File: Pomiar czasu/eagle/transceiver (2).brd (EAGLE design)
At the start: 112.4 x 62.2 mm, 65 parts, among them IC1 MEGA8-AI, IC2 LF33, IC3 LF50, U1 RFM69HW

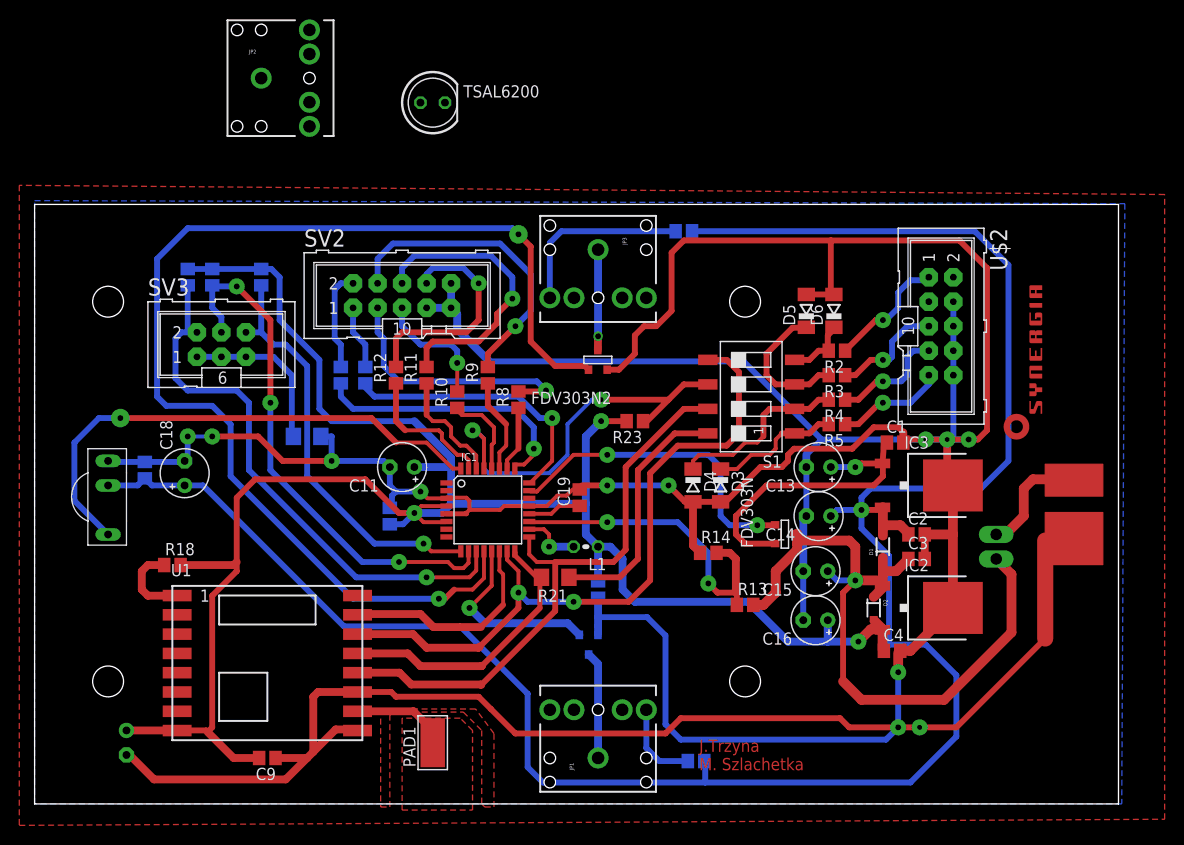
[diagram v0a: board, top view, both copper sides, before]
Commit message: RFM69:communication master->sensor works!
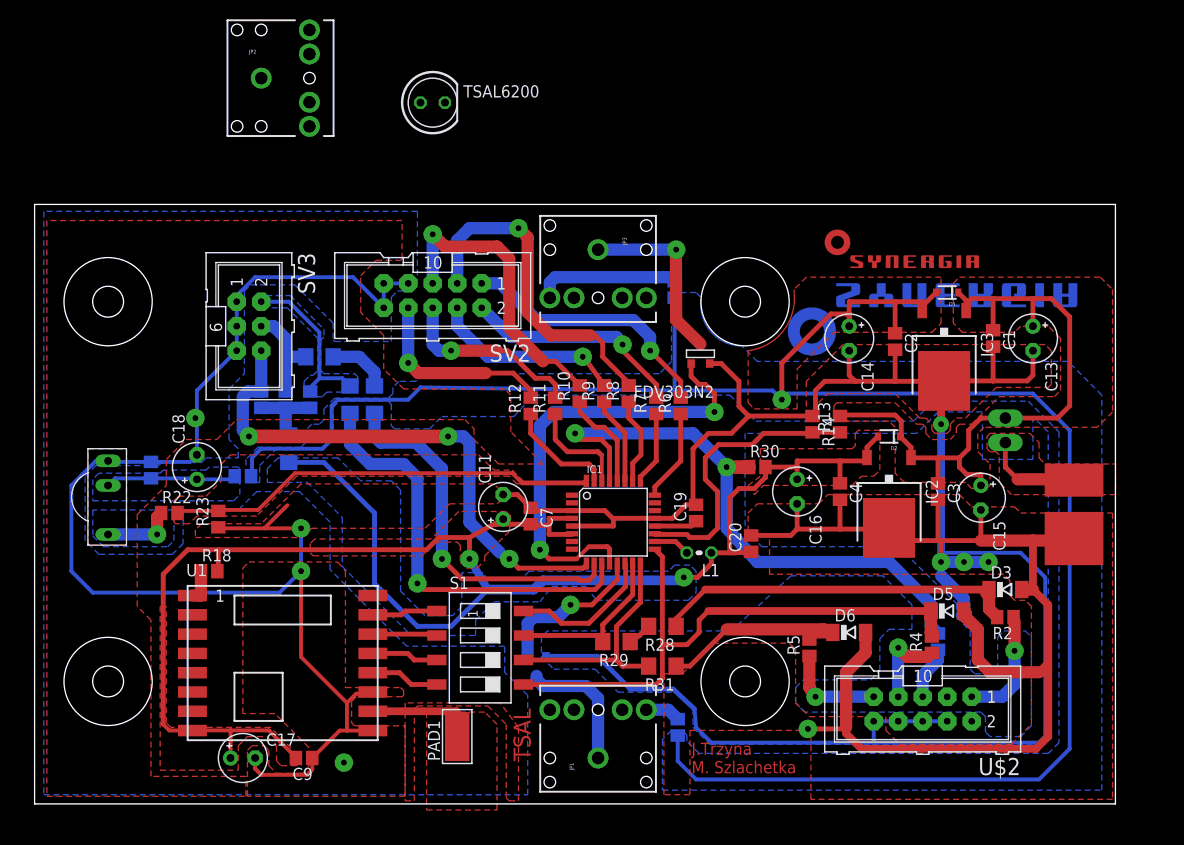
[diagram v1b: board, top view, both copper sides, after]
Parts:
- removed FDV303N: (no value), zetex:SOT-23
- added R22: 330k, resistor:R0805
- added R28, R29, R31, R32, R33, R35: 0R, rcl:R1206
- added R30: 10k, resistor:R0805
- added U$4: (no value), synergia_logo:SYNERGIA_30MM
- C1, C10, C19, C2, C20, C3, C4, C7, C9: value (none) -> 100n
- C11, C17: value (none) -> 22u
- C13, C14, C15, C16: value (none) -> 47u
- C18: value (none) -> 4,7u
- R2, R3, R4, R5: value (none) -> 330k
- R21: value 0R -> 220R; device rcl:R1206 -> resistor:R0805
- R23: value 1k -> 820k
- moved R23 44.4 mm to (19.1, 27.0), turned to 90 degrees
- moved U$2 39.7 mm to (92.1, 7.30), turned to 180 degrees
- moved S1 38.3 mm to (46.2, 13.7), turned to 270 degrees
- moved D5 34.4 mm to (94.6, 17.5), turned to 0 degrees
- moved R21 34.0 mm to (21.6, 31.4), flipped to the bottom
- moved D6 33.4 mm to (84.5, 15.2), turned to 0 degrees
- moved R6 32.9 mm to (67.0, 38.7), flipped to the top
- moved R7 32.9 mm to (64.5, 38.7), flipped to the top
- moved R2 32.7 mm to (100.6, 16.8)
- moved D3 31.4 mm to (100.6, 19.7), turned to 0 degrees
- moved R3 29.5 mm to (93.7, 14.3), flipped to the bottom, turned to 90 degrees
- moved D4 29.4 mm to (94.6, 17.5), flipped to the bottom, turned to 180 degrees
- moved U$3 28.7 mm to (81.9, 53.0), turned to 0 degrees
- moved R4 27.2 mm to (93.0, 14.0), turned to 90 degrees
- moved D1 27.2 mm to (94.6, 50.5), turned to 180 degrees
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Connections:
- removed net 5V_ENABLE: FDV303N.3, IC1.23
- removed net N$24: R21.1, S1.8
- new net N$25: C10.1, C18.+, R21.1, TSOP.V+
- new net N$33: R16.1, R33.2, SV3.4
- new net N$35: R33.1, R35.2
- new net N$36: S1.3, U1.13
- new net N$37: S1.2, U1.14
- new net N$38: S1.4, U1.12
- new net N$39: S1.1, U1.15
- net +3V3: now also R20.2, R30.2; no longer R15.2, R16.2, R17.2, R23.2
- net +5V: now also R21.2; no longer C10.2, C18.+, TSOP.V+
- net GND: now also C10.2, R23.1, SV3.1, SV3.3, SV3.5; no longer C10.1, R20.1
- net MISO: now also R31.2, S1.6; no longer R21.2, U1.13
- net MOSI: now also R29.2, S1.7; no longer S1.5, U1.14
- net N$1: now also R22.1, TSOP.OUT; no longer C1.1, C13.+, FDV303N.2, IC3.1
- net N$23: now also R15.2, R16.2, R17.2, R20.1; no longer R20.2, SV3.1, SV3.3, SV3.5
- net N$27: now also C1.1, C13.+, IC3.1; no longer FDV303N.1
- net N$29: now also R28.2, R29.1; no longer D6.C, R2.2, S1.4
- net N$30: now also D3.C, R2.2, R28.1; no longer D5.C, R3.2, S1.3
- net N$31: now also D6.C, R31.1, R5.2; no longer D4.C, R4.2, S1.2
- net N$32: now also R15.1, R32.2, SV3.2; no longer D3.C, R5.2, S1.1
- net RESET: now also D4.C, R3.2, R30.1; no longer R23.1, S1.6
- net SCK: now also D5.C, R4.2, S1.5; no longer S1.7, U1.12
- net SS: now also S1.8; no longer U1.15
- net SWITCH_DOWN: now also R32.1; no longer R15.1, SV3.2
- net SWITCH_OK: now also R35.1; no longer R16.1, SV3.4
- net TSOP_OUT: now also R22.2, R23.2; no longer TSOP.OUT
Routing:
- net LED_STRIPE: track 121.6 -> 47.7 mm
- net MOSI: track 72.4 -> 17.8 mm, vias 2 -> 0
- net 5V_ENABLE: track 33.0 -> 0.00 mm, vias 2 -> 0
- net N$1: track 33.5 -> 7.48 mm
- net N$24: track 26.0 -> 0.00 mm
- net GND: track 511.4 -> 486.3 mm, vias 12 -> 9
- net +3V3: track 209.1 -> 184.0 mm, vias 3 -> 2
- net N$30: track 14.7 -> 38.1 mm
- net LED2: track 28.3 -> 7.60 mm, vias 1 -> 0
- net N$9: track 6.66 -> 27.4 mm, vias 0 -> 1
- net RESET: track 41.9 -> 61.3 mm
- net LED1: track 28.9 -> 9.53 mm, vias 1 -> 0
- net N$13: track 12.9 -> 31.0 mm
- net SWITCH_OK: track 54.5 -> 38.2 mm, vias 3 -> 1
- net SWITCH_DOWN: track 58.6 -> 44.2 mm
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- added copper zone on layer 1, net +3V3
- added copper zone on layer 16, net +3V3
- added copper zone on layer 1, net +5V
- added copper zone on layer 16, net +5V
- added copper zone on layer 16, net N$1
- added copper zone on layer 1, net N$19
- added copper zone on layer 16, net N$25
- added copper zone on layer 1, net N$27
- added copper zone on layer 16, net N$32
- added copper zone on layer 1, net N$34
- added copper zone on layer 1, net TSOP_OUT
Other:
- board size 112.4 x 62.2 mm -> 112.1 x 62.2 mm
- board text added: "TSAL"

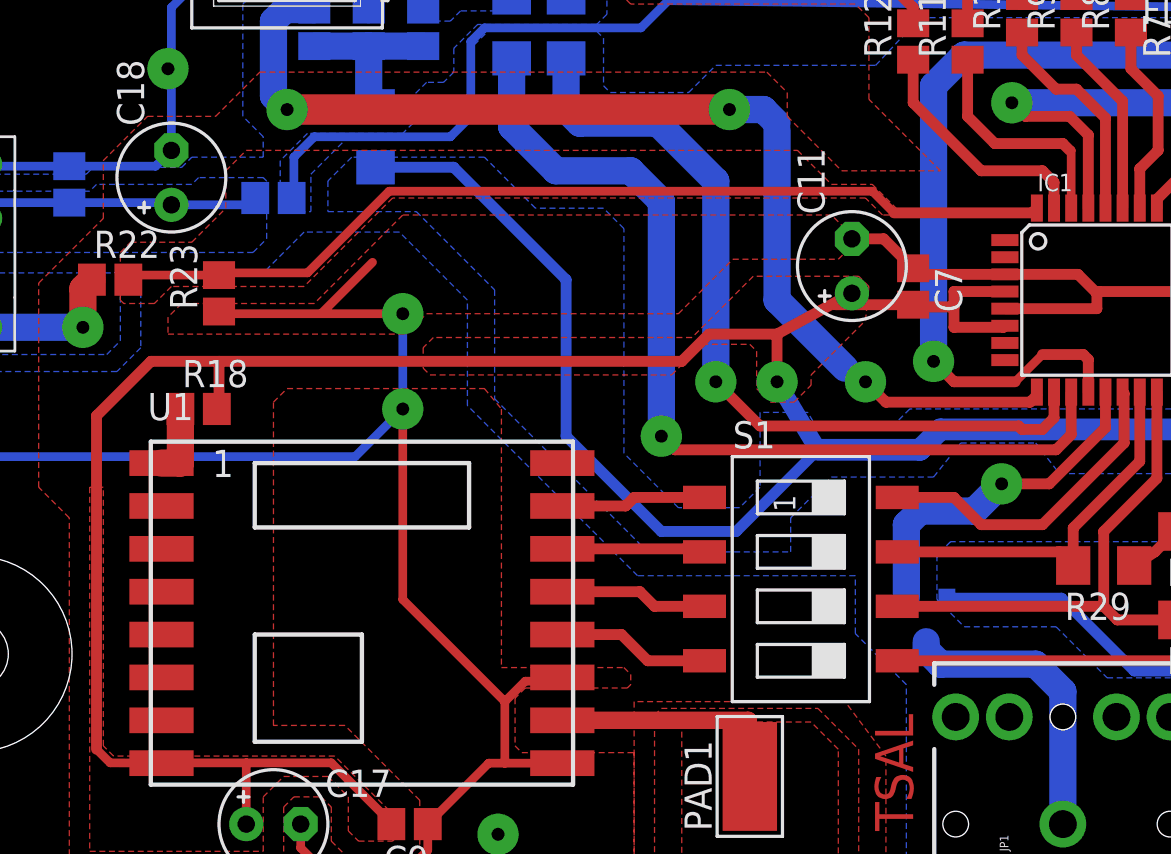
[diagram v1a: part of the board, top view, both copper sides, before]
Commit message: Channel: 442MHz(!!), ping with acknowledgement
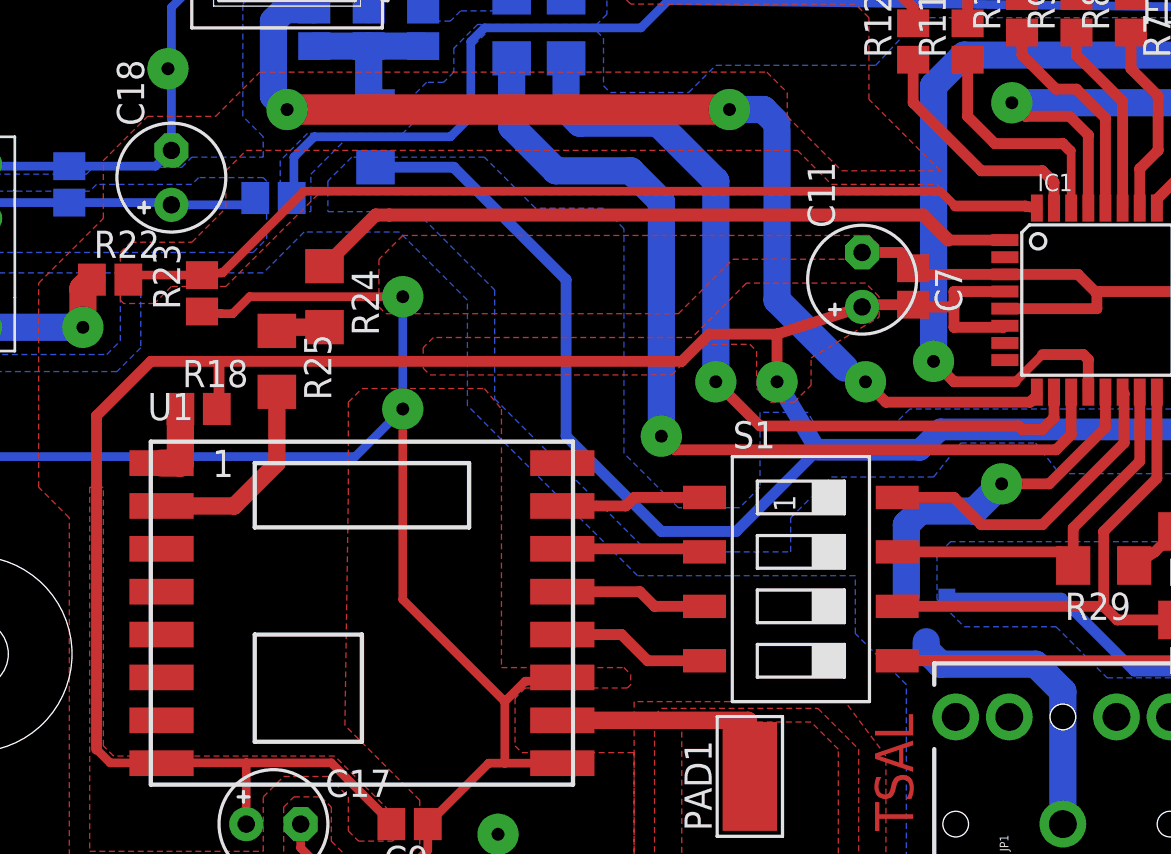
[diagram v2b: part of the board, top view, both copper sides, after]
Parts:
- added R24, R25: 0R, rcl:R1206
- moved C11 0.79 mm to (49.1, 27.6)
- moved R23 0.79 mm to (18.3, 27.0)
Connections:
- new net DIO0: IC1.1, R24.1
- new net N$24: R24.2, R25.1
- new net N$45: R25.2, U1.2
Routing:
- net DIO0: track 0.00 -> 33.4 mm
- net N$45: track 0.00 -> 9.54 mm
- net N$24: track 0.00 -> 2.29 mm
- net GND: track 486.3 -> 484.1 mm
- net +3V3: track 184.0 -> 182.1 mm

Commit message: final v1.0
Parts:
- removed R23: 820k, resistor:R0805
- added D7: (no value), diode:SOD80C
- R40: value 330k -> 220R
- moved R1 70.2 mm to (35.1, 68.1), turned to 0 degrees
- renumbered R22 to R40
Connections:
- net +5V: now also JP1.TIP; no longer R1.2
- net GND: now also D7.A; no longer R23.1
- net N$3: now also R1.2; no longer TSAL6200.A
- net N$8: now also TSAL6200.A; no longer JP1.TIP
- net TSOP_OUT: now also D7.C; no longer R23.2
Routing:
- net +5V: track 212.4 -> 216.9 mm
- net N$8: track 3.66 -> 0.00 mm
- net TSOP_OUT: track 44.4 -> 43.1 mm
- net GND: track 484.1 -> 483.5 mm
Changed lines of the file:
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@@
 <element name="TSOP" library="tsop" package="TSOP17XX" value="TSOP1736" x="7.62" y="29.21" rot="R270"/>
 <element name="TSAL6200" library="led" package="LED5MM" value="" x="41.275" y="70.1675"/>
-<element name="R1" library="resistor" package="R0805" value="36,5R" x="66.675" y="5.3975" rot="MR270"/>
+<element name="R1" library="resistor" package="R0805" value="36,5R" x="35.08375" y="68.10375" rot="MR0"/>
 <element name="U1" library="SparkFun-RF" package="RFM69W-XXXS2" value="RFM69HW" x="25.7175" y="12.065"/>
 <element name="U$2" library="con-harting-ml" package="ML10" value="" x="92.075" y="7.3025" rot="R180">
@@
 </element>
 <element name="R20" library="rcl" package="R1206" value="0R" x="26.3525" y="34.29" rot="MR270"/>
-<element name="R22" library="resistor" package="R0805" value="330k" x="13.97" y="27.6225"/>
+<element name="R40" library="resistor" package="R0805" value="220R" x="13.97" y="27.6225"/>
 <element name="R21" library="resistor" package="R0805" value="220R" x="21.59" y="31.4325" rot="MR180"/>
-<element name="R23" library="resistor" package="R0805" value="820k" x="18.25625" y="26.9875" rot="R90"/>
 <element name="R28" library="rcl" package="R1206" value="0R" x="65.0875" y="15.875" rot="R180"/>
 <element name="R31" library="rcl" package="R1206" value="0R" x="65.0875" y="11.7475" rot="R180"/>
@@
 <element name="R24" library="rcl" package="R1206" value="0R" x="23.97125" y="26.82875" rot="R270"/>
 <element name="R25" library="rcl" package="R1206" value="0R" x="21.74875" y="23.8125" rot="R270"/>
+<element name="D7" library="diode" package="SOD80C" value="" x="17.30375" y="25.55875"/>
 </elements>
 <signals>
 <signal name="+5V">
 <contactref element="R19" pad="2"/>
-<contactref element="R1" pad="2"/>
 <contactref element="C2" pad="1"/>
 <contactref element="C14" pad="+"/>
@@
 <wire x1="76.5175" y1="40.3225" x2="77.47" y2="39.37" width="0.4064" layer="16"/>
 <wire x1="66.3575" y1="49.95" x2="66.3575" y2="40.3225" width="0.4064" layer="16"/>
-<wire x1="66.675" y1="4.5475" x2="66.675" y2="1.905" width="0.4064" layer="16"/>
-<wire x1="66.675" y1="1.905" x2="68.58" y2="0" width="0.4064" layer="16"/>
+<wire x1="66.675" y1="1.905" x2="67.071875" y2="1.508125" width="0.4064" layer="16"/>
+<wire x1="67.071875" y1="1.508125" x2="68.58" y2="0" width="0.4064" layer="16"/>
 <wire x1="68.58" y1="0" x2="104.14" y2="0" width="0.4064" layer="16"/>
 <wire x1="104.14" y1="0" x2="107.315" y2="3.175" width="0.4064" layer="16"/>
@@
 </polygon>
 <polygon width="0.2032" layer="16">
-<vertex x="66.04" y="5.08"/>
-<vertex x="65.0875" y="4.1275"/>
-<vertex x="65.0875" y="-1.11125"/>
+<vertex x="62.5475" y="8.09625"/>
+<vertex x="62.5475" y="-0.9525"/>
 <vertex x="110.64875" y="-1.11125"/>
 <vertex x="110.64875" y="39.84625"/>
@@
 <vertex x="106.20375" y="3.81"/>
 <vertex x="105.0925" y="2.69875"/>
-<vertex x="68.8975" y="2.69875"/>
-<vertex x="67.6275" y="3.96875"/>
-<vertex x="67.6275" y="4.60375"/>
+<vertex x="69.5325" y="2.69875"/>
 <vertex x="67.15125" y="5.08"/>
-</polygon>
+<vertex x="67.15125" y="6.50875"/>
+<vertex x="65.56375" y="8.09625"/>
+</polygon>
+<contactref element="JP1" pad="TIP"/>
+<wire x1="63.42" y1="7.2225" x2="63.42" y2="5.16" width="1.016" layer="16"/>
+<wire x1="63.42" y1="5.16" x2="67.071875" y2="1.508125" width="1.016" layer="16"/>
 </signal>
 <signal name="+3V3">
@@
 <signal name="TSOP_OUT">
 <contactref element="IC1" pad="32"/>
-<contactref element="R22" pad="2"/>
-<contactref element="R23" pad="2"/>
+<contactref element="R40" pad="2"/>
 <wire x1="14.82" y1="27.6225" x2="15.035" y2="27.8375" width="0.4064" layer="1"/>
-<wire x1="15.035" y1="27.8375" x2="18.25625" y2="27.8375" width="0.4064" layer="1"/>
-<wire x1="18.25625" y1="27.8375" x2="19.1525" y2="27.94" width="0.4064" layer="1"/>
 <wire x1="19.1525" y1="27.94" x2="19.20875" y2="27.94" width="0.4064" layer="1"/>
 <wire x1="19.20875" y1="27.94" x2="23.01875" y2="31.75" width="0.4064" layer="1"/>
@@
 <wire x1="57.2075" y1="30.9626" x2="56.6674" y2="31.0575" width="0.508" layer="1"/>
 <wire x1="56.6674" y1="31.0575" x2="53.3975" y2="31.0575" width="0.508" layer="1"/>
+<contactref element="D7" pad="C"/>
+<wire x1="15.60375" y1="25.55875" x2="15.60375" y2="27.57625" width="0.4064" layer="1"/>
+<wire x1="15.60375" y1="27.57625" x2="15.5575" y2="27.6225" width="0.4064" layer="1"/>
+<wire x1="15.5575" y1="27.6225" x2="14.82" y2="27.6225" width="0.4064" layer="1"/>
 </signal>
 <signal name="MOSI">
@@
 </polygon>
 </signal>
-<signal name="N$8">
-<contactref element="R1" pad="1"/>
-<contactref element="JP1" pad="TIP"/>
-<wire x1="63.42" y1="7.2225" x2="65.7" y2="7.2225" width="1.27" layer="16"/>
-<wire x1="65.7" y1="7.2225" x2="66.675" y2="6.2475" width="1.27" layer="16"/>
-</signal>
 <signal name="N$14">
 <contactref element="JP1" pad="SLEEVE"/>
@@
 <wire x1="7.7225" y1="32.9175" x2="7.62" y2="33.02" width="0.6096" layer="16"/>
 <contactref element="C18" pad="-"/>
-<contactref element="R23" pad="1"/>
 <contactref element="C10" pad="2"/>
 <contactref element="SV3" pad="5"/>
@@
 <wire x1="20.955" y1="44.45" x2="20.955" y2="46.99" width="0.4064" layer="16"/>
 <wire x1="20.955" y1="46.99" x2="20.955" y2="49.53" width="0.4064" layer="16"/>
-<wire x1="18.25625" y1="26.1375" x2="19.1525" y2="26.035" width="0.4064" layer="1"/>
 <wire x1="36.195" y1="48.895" x2="33.02" y2="52.07" width="0.4064" layer="16"/>
 <wire x1="33.02" y1="52.07" x2="22.86" y2="52.07" width="0.4064" layer="16"/>
@@
 <wire x1="68.58" y1="5.3975" x2="70.1675" y2="3.81" width="0.4064" layer="16"/>
 <wire x1="70.1675" y1="3.81" x2="86.995" y2="3.81" width="0.4064" layer="16"/>
-<wire x1="19.1525" y1="26.035" x2="19.685" y2="26.035" width="0.4064" layer="1"/>
-<wire x1="19.685" y1="26.035" x2="20.47875" y2="26.82875" width="0.4064" layer="1"/>
-<wire x1="20.47875" y1="26.82875" x2="27.6225" y2="26.82875" width="0.4064" layer="1"/>
+<wire x1="20.27375" y1="26.82875" x2="27.6225" y2="26.82875" width="0.4064" layer="1"/>
 <wire x1="35.845" y1="8.89" x2="33.3375" y2="8.89" width="0.4064" layer="1"/>
 <wire x1="33.3375" y1="8.89" x2="32.385" y2="7.9375" width="0.4064" layer="1"/>
@@
 <vertex x="103.34625" y="5.55625"/>
 <vertex x="102.235" y="4.445"/>
-<vertex x="99.06" y="4.445"/>
-<vertex x="98.58375" y="4.92125"/>
-<vertex x="98.58375" y="6.50875"/>
-<vertex x="98.1075" y="6.985"/>
+<vertex x="96.04375" y="4.445"/>
+<vertex x="95.5675" y="4.92125"/>
+<vertex x="95.5675" y="6.50875"/>
+<vertex x="95.09125" y="6.985"/>
 <vertex x="79.85125" y="6.985"/>
 <vertex x="78.89875" y="7.9375"/>
@@
 <vertex x="58.1025" y="11.43"/>
 <vertex x="60.48375" y="9.04875"/>
-<vertex x="66.51625" y="9.04875"/>
-<vertex x="68.2625" y="7.3025"/>
+<vertex x="66.19875" y="9.04875"/>
+<vertex x="68.2625" y="6.985"/>
 <vertex x="68.2625" y="5.3975"/>
 <vertex x="70.00875" y="3.65125"/>
@@
 <wire x1="51.435" y1="28.155" x2="51.72" y2="27.87" width="0.508" layer="1"/>
 <wire x1="51.72" y1="27.87" x2="55.7149" y2="27.87" width="0.508" layer="1"/>
+<contactref element="D7" pad="A"/>
+<wire x1="20.27375" y1="26.82875" x2="19.00375" y2="25.55875" width="0.4064" layer="1"/>
 </signal>
 <signal name="N$15">
@@
 <wire x1="65.9375" y1="52.07" x2="66.3575" y2="51.65" width="1.27" layer="16"/>
 </signal>
-<signal name="N$3">
-<contactref element="JP2" pad="TIP"/>
-<contactref element="TSAL6200" pad="A"/>
-<wire x1="28.495" y1="67.7075" x2="40.005" y2="70.1675" width="0" layer="19" extent="1-1"/>
-</signal>
 <signal name="N$1">
 <contactref element="TSOP" pad="OUT"/>
-<contactref element="R22" pad="1"/>
+<contactref element="R40" pad="1"/>
 <wire x1="13.12" y1="27.6225" x2="12.7" y2="27.2025" width="1.27" layer="1"/>
 <wire x1="12.7" y1="27.2025" x2="12.7" y2="25.4" width="1.27" layer="1"/>
@@
 <wire x1="19.76375" y1="17.065" x2="16.3675" y2="17.065" width="0.8128" layer="1"/>
 </signal>
+<signal name="N$3">
+<contactref element="JP2" pad="TIP"/>
+<contactref element="R1" pad="2"/>
+<wire x1="28.495" y1="67.7075" x2="34.23375" y2="68.10375" width="0" layer="19" extent="16-16"/>
+</signal>
+<signal name="N$8">
+<contactref element="TSAL6200" pad="A"/>
+<contactref element="R1" pad="1"/>
+<wire x1="35.93375" y1="68.10375" x2="40.005" y2="70.1675" width="0" layer="19" extent="16-16"/>
+</signal>
 </signals>
